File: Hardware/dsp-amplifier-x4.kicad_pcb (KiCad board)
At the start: 4 copper layers, 182 x 90 mm, 167 parts, among them J1 USBi, J10 Conn_Coaxial, J2 EXT, J3 Raspberry_Pi_2_3, J4 Screw_Terminal_01x02, J5 Screw_Terminal_01x02, J6 Screw_Terminal_01x02, J7 Screw_Terminal_01x02, J8 USB_B, J9 Conn_Coaxial, P1 Conn_WallPlug, Q1 STD2805, T1 DA100J, U1 ADAU1452, U10 25LCxxx, U2 TPS54308, U3 TPS54308, U4 AMS1117-3.3, U5 SI53365, U6 TAS5760MDCAR, U7 TAS5760MDCAR, U8 USBLC6-2SC6, U9 PCM2707, X1 ASV-24.576MHz-EJ-T, Y1 12 MHz

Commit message: release candidate 1, drc clean
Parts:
- moved C1 2.83 mm to (98.5, 84.2)
- moved C22 1.77 mm to (98.5, 81.8)
- moved J9 0.75 mm to (89.0, 77.0)
- moved J10 0.25 mm to (73.0, 77.0)
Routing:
- net /DVDD: track 57.4 -> 51.6 mm
- net Net-(C79-Pad1): track 13.6 -> 11.1 mm
- net +3V3: track 119.7 -> 121.7 mm
- net /GAIN0: track 53.6 -> 52.0 mm
- net GND: track 240.5 -> 239.4 mm
- net +3.3VA: track 30.6 -> 30.5 mm, vias 17 -> 18

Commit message: new sockets
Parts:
- J4, J5, J6, J7, P1: footprint TerminalBlock:TerminalBlock_Wuerth_691311400102_P7.62mm -> terminal_connectors:wuerth_691216410002
- moved P1 4.12 mm to (237.2, 127.0), turned to 270 degrees
- moved J4 4.00 mm to (172.0, 123.5), turned to 90 degrees
- moved J5 4.00 mm to (172.0, 140.5), turned to 90 degrees
- moved J6 3.81 mm to (172.0, 89.1), turned to 90 degrees
- moved J7 3.75 mm to (172.0, 106.0), turned to 90 degrees
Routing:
- net /Power/AC_N: track 33.2 -> 33.8 mm
- net /Power/AC_L: track 21.1 -> 21.7 mm

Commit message: production v0.1 with gerber
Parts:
- added TP1: TestPoint, TestPoint:TestPoint_Pad_D1.0mm, F.Cu at (108.5, 115.0)
- added TP2: NCS, TestPoint:TestPoint_Pad_D1.0mm, F.Cu at (92.0, 142.0)
- added TP3: MISO, TestPoint:TestPoint_Pad_D1.0mm, F.Cu at (91.5, 133.8)
- added TP4: MOSI, TestPoint:TestPoint_Pad_D1.0mm, F.Cu at (94.0, 133.8)
- added TP5: SCLK, TestPoint:TestPoint_Pad_D1.0mm, F.Cu at (89.0, 133.8)
- moved R4 5.59 mm to (104.5, 96.2), turned to 180 degrees
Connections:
- Q1 pad 3: +3.3VA -> +3V3
- R4 pad 1: +3.3VA -> +3V3
- U1 pad 23: (no net) -> Net-(TP1-Pad1)
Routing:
- net Net-(TP1-Pad1): track 0.00 -> 8.83 mm
- net +3.3VA: track 30.5 -> 24.5 mm, vias 18 -> 16
- net /VDRIVE: track 11.1 -> 7.33 mm
- net +3V3: track 121.7 -> 124.7 mm
- net /PI_SCLK0: track 110.1 -> 112.8 mm
- net /PI_MOSI0: track 92.1 -> 94.8 mm
- net /PI_MISO0: track 105.1 -> 107.9 mm
- added copper zone on In2.Cu, net +3.3VA
- added copper zone on In2.Cu, net +3V3
- added copper zone on In2.Cu, net +5VD
- added copper zone on In2.Cu, net /DVDD
- removed copper zone on In1.Cu, net +3.3VA
- removed copper zone on In1.Cu, net +3V3
- removed copper zone on In1.Cu, net +5VD
- removed copper zone on In1.Cu, net /DVDD
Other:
- rule pad_to_mask_clearance: 0.2 -> 0
- board text added: "For 24V DC"
- board text added: "stärga v0.1"
- board text removed: "soundi v0.1"

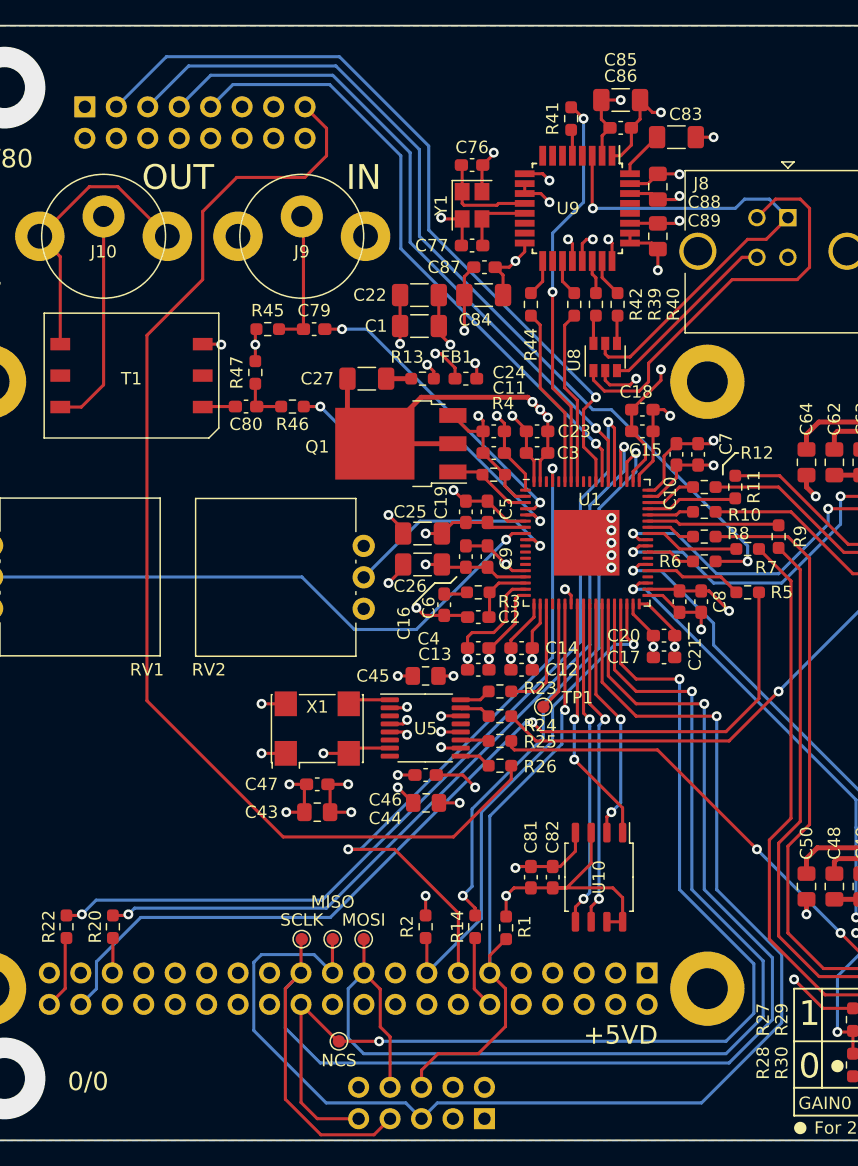
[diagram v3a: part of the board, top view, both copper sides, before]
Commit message: fixed usbi/ext header positions
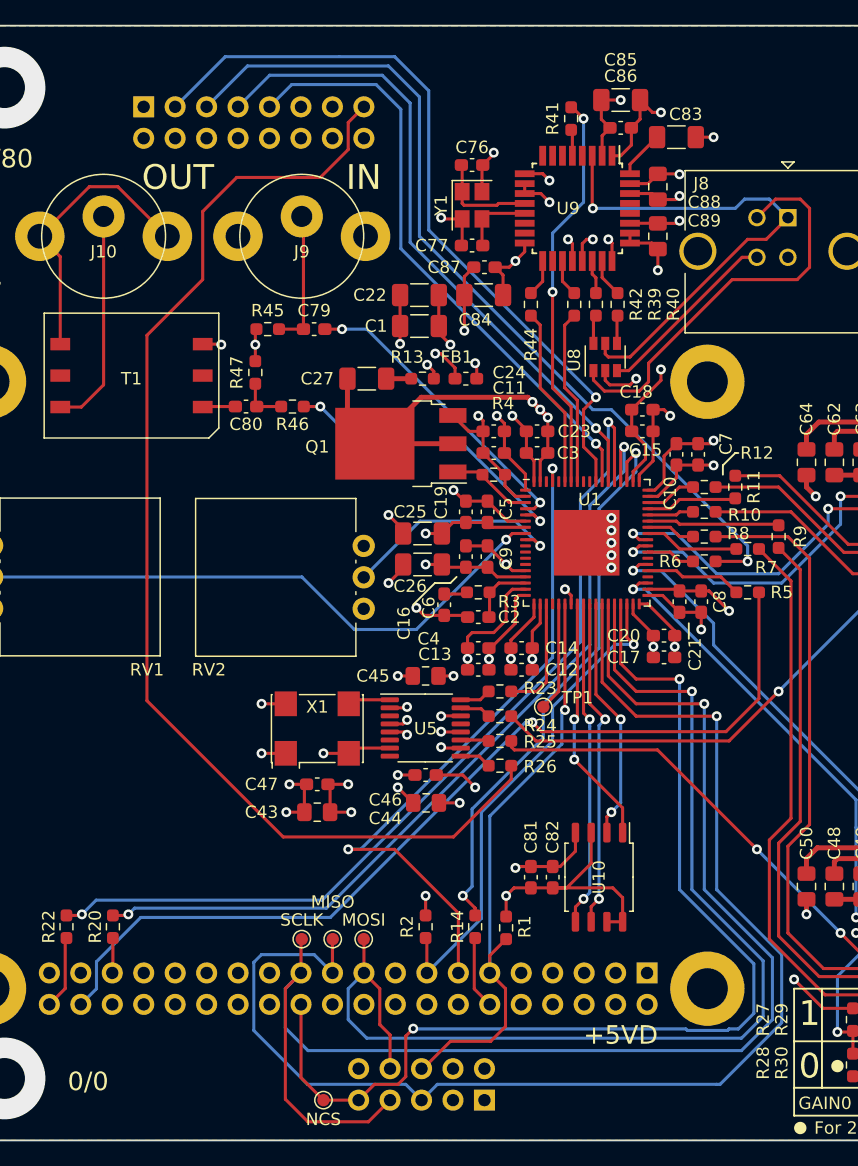
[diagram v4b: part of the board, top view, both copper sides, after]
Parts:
- moved TP2 4.91 mm to (90.8, 146.8)
- moved J2 4.75 mm to (76.2, 66.5)
- moved J1 1.50 mm to (103.8, 146.8)
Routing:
- net +24V: track 126.1 -> 121.5 mm
- net /PI_NCE0: track 91.4 -> 87.7 mm
- net /PI_MOSI0: track 94.8 -> 91.4 mm
- net /EXT_LRCLK: track 51.5 -> 49.0 mm
- net /EXT_BCLK: track 55.5 -> 53.1 mm
- net /EXT_MDO: track 73.8 -> 71.5 mm
- net /EXT_MDI: track 63.4 -> 61.2 mm
- net /DSP_NRESET: track 50.1 -> 48.7 mm
- net /EXT_MCLK: track 94.9 -> 96.1 mm
- net /PI_MISO0: track 107.9 -> 106.7 mm
- net /PI_SCLK0: track 112.8 -> 111.8 mm
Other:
- board text added: "stärga v0.2"
- board text removed: "stärga v0.1"

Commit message: hardware bugfixes
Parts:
- added R33: 1M, Resistor_SMD:R_0603_1608Metric_Pad0.98x0.95mm_HandSolder, F.Cu at (102.8, 74.2)
- added R34: 1.5k, Resistor_SMD:R_0603_1608Metric_Pad0.98x0.95mm_HandSolder, F.Cu at (117.2, 81.5)
- added R40: 1.5k, Resistor_SMD:R_0603_1608Metric_Pad0.98x0.95mm_HandSolder, F.Cu at (103.8, 77.0)
- added U2: TSOP583xx, OptoDevice:Vishay_MINICAST-3Pin, F.Cu at (113.2, 145.2)
- C58, C59, C60, C61, C72, C73, C74, C75: footprint Capacitor_SMD:C_0603_1608Metric_Pad1.08x0.95mm_HandSolder -> Capacitor_SMD:C_0805_2012Metric_Pad1.18x1.45mm_HandSolder
- RV1, RV2: footprint Potentiometer_THT:Potentiometer_Vishay_248GJ-249GJ_Single_Vertical -> Potentiometer_THT:Potentiometer_Bourns_PTV09A-1_Single_Vertical
- moved RV1 13.3 mm to (76.2, 102.0), turned to 180 degrees
- moved C76 3.02 mm to (100.0, 70.0)
- moved C77 3.02 mm to (100.0, 76.5)
- moved Y1 3.02 mm to (100.0, 73.2)
- moved C88 2.01 mm to (107.2, 128.8)
- moved C16 1.75 mm to (104.0, 102.9)
- moved C9 1.75 mm to (102.2, 102.9)
- moved C87 1.50 mm to (109.0, 128.8)
- moved C59 0.29 mm to (165.8, 126.3)
- moved C60 0.29 mm to (165.8, 141.5)
- moved C58 0.25 mm to (165.8, 122.2)
- moved C61 0.25 mm to (165.8, 137.5)
- moved C72 0.25 mm to (165.8, 88.0)
- moved C73 0.25 mm to (165.8, 92.0)
- moved C74 0.25 mm to (165.8, 107.2)
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- renumbered C83 to C78, C84 to C79, C85 to C80, C86 to C81, C87 to C82, C88 to C83, C89 to C84, C79 to C85, C80 to C86, C81 to C87, C82 to C88, R20 to R15, R22 to R16, R23 to R17, R24 to R18, R25 to R19, R26 to R20, R27 to R21, R28 to R22, R29 to R23, R30 to R24, R31 to R25, R32 to R26, R33 to R27, R34 to R28, R35 to R29, R36 to R30, R37 to R31, R38 to R32, R39 to R35, R40 to R36, R41 to R37, R42 to R38, R44 to R39, R45 to R41, R46 to R42, R47 to R43, U9 to U10, U10 to U11, U2 to U3, U3 to U4, U4 to U5, U5 to U6, U6 to U7, U7 to U8, U8 to U9
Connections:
- J2 pad 1: +24V -> +5VA
- J3 pad 1: (no net) -> PI_3V3
- J3 pad 3: (no net) -> /IR_INPUT
- U10 pad 11: +3V3 -> (no net)
- U10 pad 15: (no net) -> Net-(R40-Pad1)
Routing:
- net +5VA: track 26.3 -> 218.9 mm, vias 0 -> 3
- net +24V: track 121.5 -> 37.6 mm
- net GND: track 239.4 -> 228.1 mm, vias 116 -> 115
- net PI_3V3: track 0.00 -> 10.4 mm
- net /VPOT0: track 48.0 -> 38.5 mm
- net /IR_INPUT: track 0.00 -> 9.35 mm
- net Net-(C76-Pad1): track 8.30 -> 11.4 mm
- net Net-(C77-Pad1): track 5.81 -> 8.71 mm
- net Net-(R40-Pad1): track 0.00 -> 2.44 mm
- net /EXT_MCLK: track 96.1 -> 94.1 mm
- net +3V3: track 124.7 -> 122.7 mm, vias 29 -> 30
- net /USB I2S/USB-DP: track 3.11 -> 4.98 mm
- net /PI_MISO0: track 106.7 -> 107.9 mm
- net Net-(C33-Pad1): track 8.22 -> 7.00 mm
- net Net-(C32-Pad1): track 8.22 -> 7.00 mm
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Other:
- board text added: "+5VA supplied"
- board text added: "IR RX"
- board text added: "stärga v1"
- board text removed: "stärga v0.2"

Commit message: various bugfixes
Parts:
- removed TP1: TestPoint, TestPoint:TestPoint_Pad_D1.0mm
- removed TP2: NCS, TestPoint:TestPoint_Pad_D1.0mm
- removed TP3: MISO, TestPoint:TestPoint_Pad_D1.0mm
- removed TP4: MOSI, TestPoint:TestPoint_Pad_D1.0mm
- removed TP5: SCLK, TestPoint:TestPoint_Pad_D1.0mm
- FB1: value 600/100M -> BLM18SP601SZ1D (600/100M)
- RV1, RV2: value R_POT -> PTV09A-1020F-B203
- moved FB1 2.83 mm to (100.2, 86.5)
- moved U2 2.25 mm to (115.5, 145.2)
- moved C53 0.75 mm to (149.8, 115.5)
- moved C83 0.50 mm to (117.8, 72.5)
- turned R33 to 90 degrees
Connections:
- R33 pad 1: Net-(C76-Pad1) -> Net-(C77-Pad1)
- R33 pad 2: Net-(C77-Pad1) -> Net-(C76-Pad1)
- R34 pad 2: +3V3 -> VBUS
- U1 pad 23: Net-(TP1-Pad1) -> (no net)
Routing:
- net Net-(TP1-Pad1): track 8.83 -> 0.00 mm
- net /PI_SCLK0: track 112.4 -> 105.8 mm
- net +5VA: track 218.9 -> 225.4 mm, vias 3 -> 5
- net /PI_MOSI0: track 92.2 -> 86.7 mm
- net /SPDIF_IN: track 24.6 -> 28.4 mm
- net GND: track 228.1 -> 225.7 mm, vias 115 -> 116
- net VBUS: track 41.3 -> 43.3 mm
- net /PI_NCE0: track 88.5 -> 89.6 mm, vias 2 -> 1
- net PI_3V3: track 10.4 -> 11.3 mm
- net /IR_INPUT: track 9.35 -> 10.3 mm
- net +3V3: track 122.7 -> 121.9 mm, vias 30 -> 31
- net /PI_MISO0: track 107.9 -> 107.3 mm
- net /AMP1_NSPK_SD: track 41.0 -> 40.4 mm
- net +3.3VA: track 24.5 -> 24.6 mm, vias 16 -> 18
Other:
- board text added: "VAUX0"
- board text added: "VAUX1"

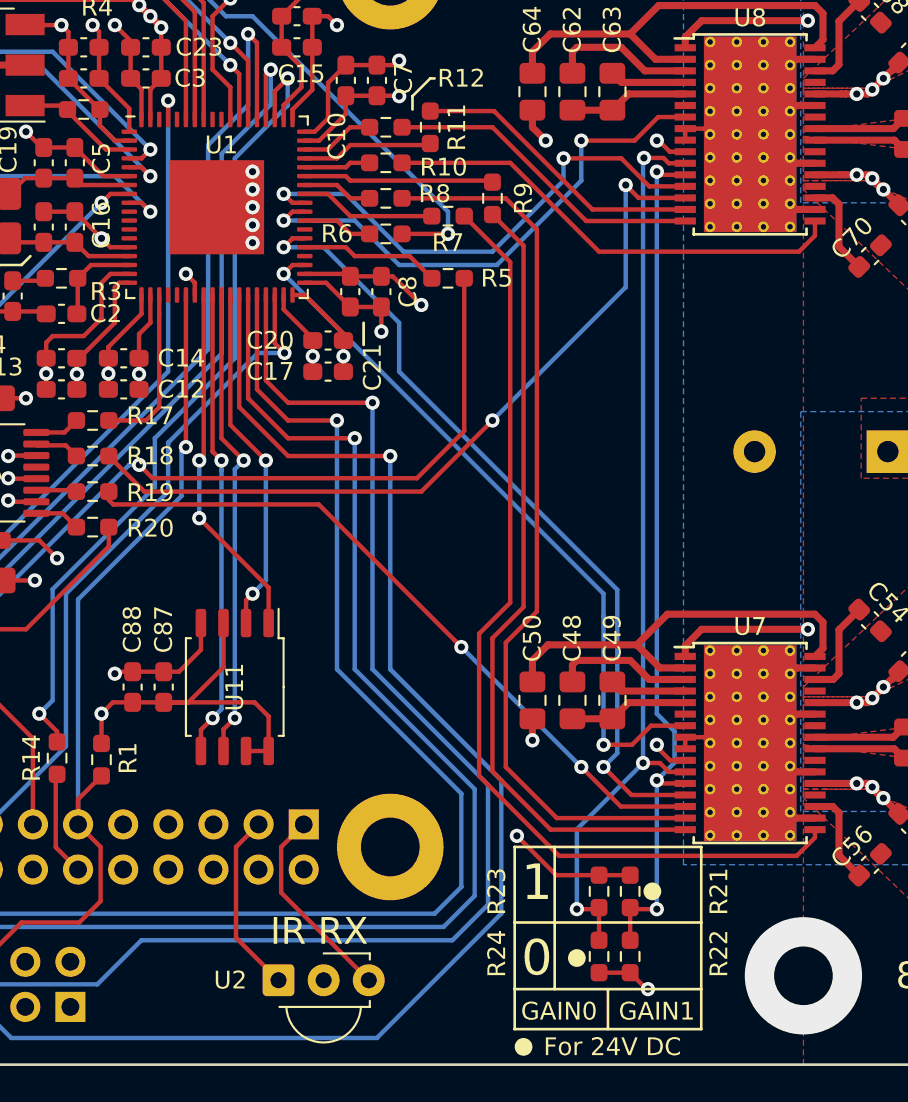
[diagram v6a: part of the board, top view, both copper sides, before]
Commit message: software gain control
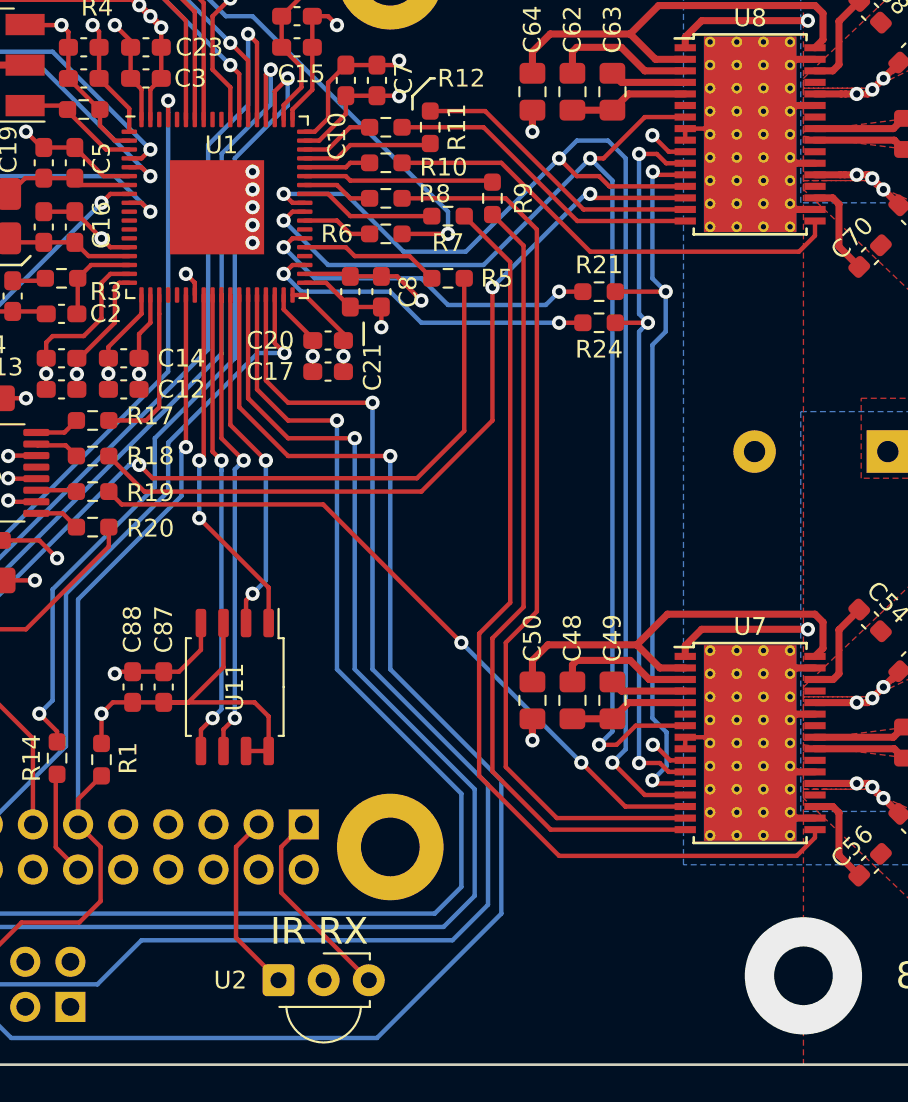
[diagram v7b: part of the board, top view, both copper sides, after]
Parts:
- removed R22, R23: DNP, Resistor_SMD:R_0603_1608Metric_Pad0.98x0.95mm_HandSolder
- moved R24 35.7 mm to (133.5, 108.2), turned to 180 degrees
- moved R21 33.8 mm to (133.5, 106.5), turned to 180 degrees
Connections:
- R21 pad 2: +3V3 -> /GAIN1_OUT
- R24 pad 1: GND -> /GAIN0
- R24 pad 2: /GAIN0 -> /GAIN0_OUT
- U1 pad 39: /AMP1_NSPK_SD -> /GAIN0_OUT
- U1 pad 42: /AMP1_SPK_SLEEP -> /GAIN1_OUT
- U1 pad 45: /AMP2_NSPK_SD -> /AMP_NSPK_SD
- U1 pad 46: /AMP2_SPK_SLEEP -> /AMP_SPK_SLEEP
- U7 pad 13: /AMP1_SPK_SLEEP -> /AMP_SPK_SLEEP
- U7 pad 7: /AMP1_NSPK_SD -> /AMP_NSPK_SD
- U8 pad 13: /AMP2_SPK_SLEEP -> /AMP_SPK_SLEEP
- U8 pad 7: /AMP2_NSPK_SD -> /AMP_NSPK_SD
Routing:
- net /AMP_SPK_SLEEP: track 0.00 -> 71.9 mm, vias 0 -> 3
- net /AMP_NSPK_SD: track 0.00 -> 67.6 mm, vias 0 -> 3
- net /AMP1_SPK_SLEEP: track 45.3 -> 0.00 mm, vias 2 -> 0
- net /AMP1_NSPK_SD: track 40.4 -> 0.00 mm, vias 2 -> 0
- net /AMP2_NSPK_SD: track 29.8 -> 0.00 mm, vias 2 -> 0
- net /AMP2_SPK_SLEEP: track 28.9 -> 0.00 mm, vias 2 -> 0
- net /GAIN1_OUT: track 0.00 -> 19.9 mm, vias 0 -> 2
- net /GAIN0_OUT: track 0.00 -> 19.4 mm, vias 0 -> 2
- net /GAIN0: track 52.0 -> 42.2 mm
- net +3V3: track 121.9 -> 115.1 mm, vias 31 -> 30
- net /GAIN1: track 49.0 -> 42.2 mm
- net GND: track 225.7 -> 221.5 mm, vias 116 -> 115
- net /AMP2_CLOCK: track 44.1 -> 44.7 mm
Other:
- board text removed: "0"
- board text removed: "1"
- board text removed: "For 24V DC"
- board text removed: "GAIN0"
- board text removed: "GAIN1"

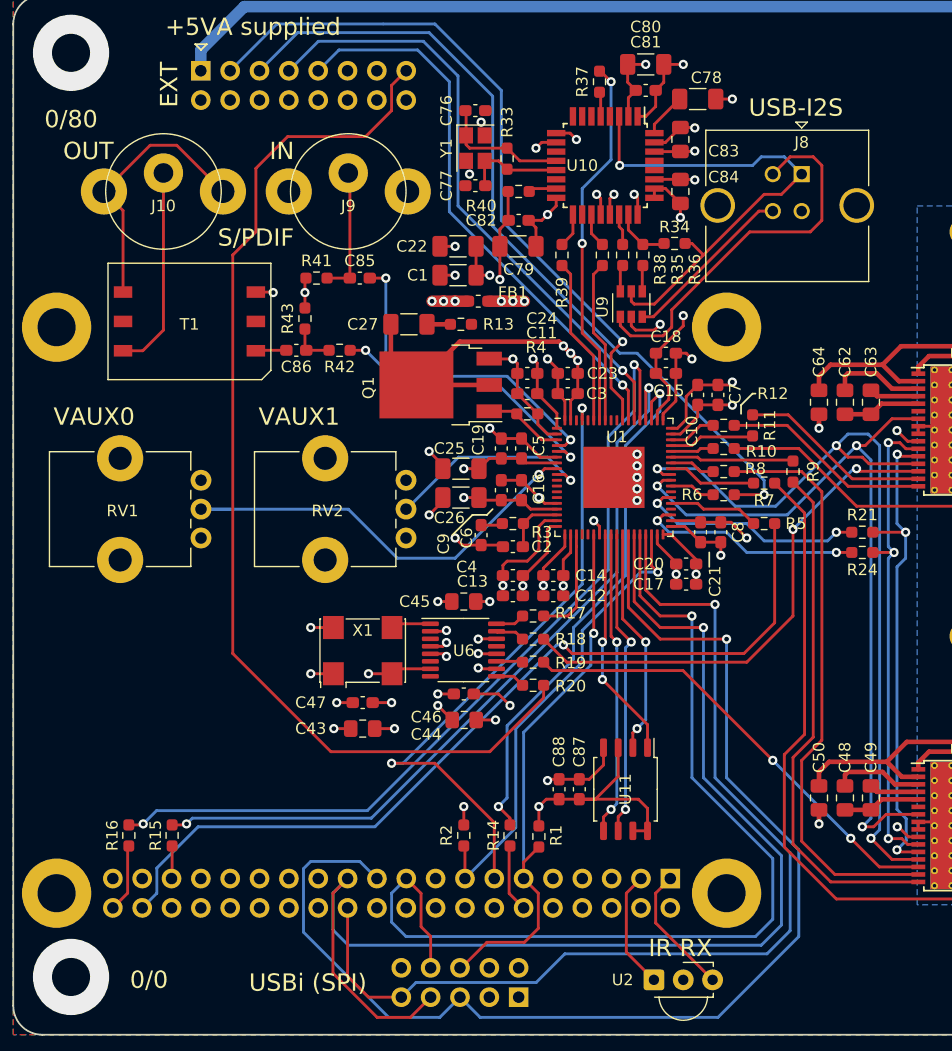
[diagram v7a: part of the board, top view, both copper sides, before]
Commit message: connect pi i2c to header
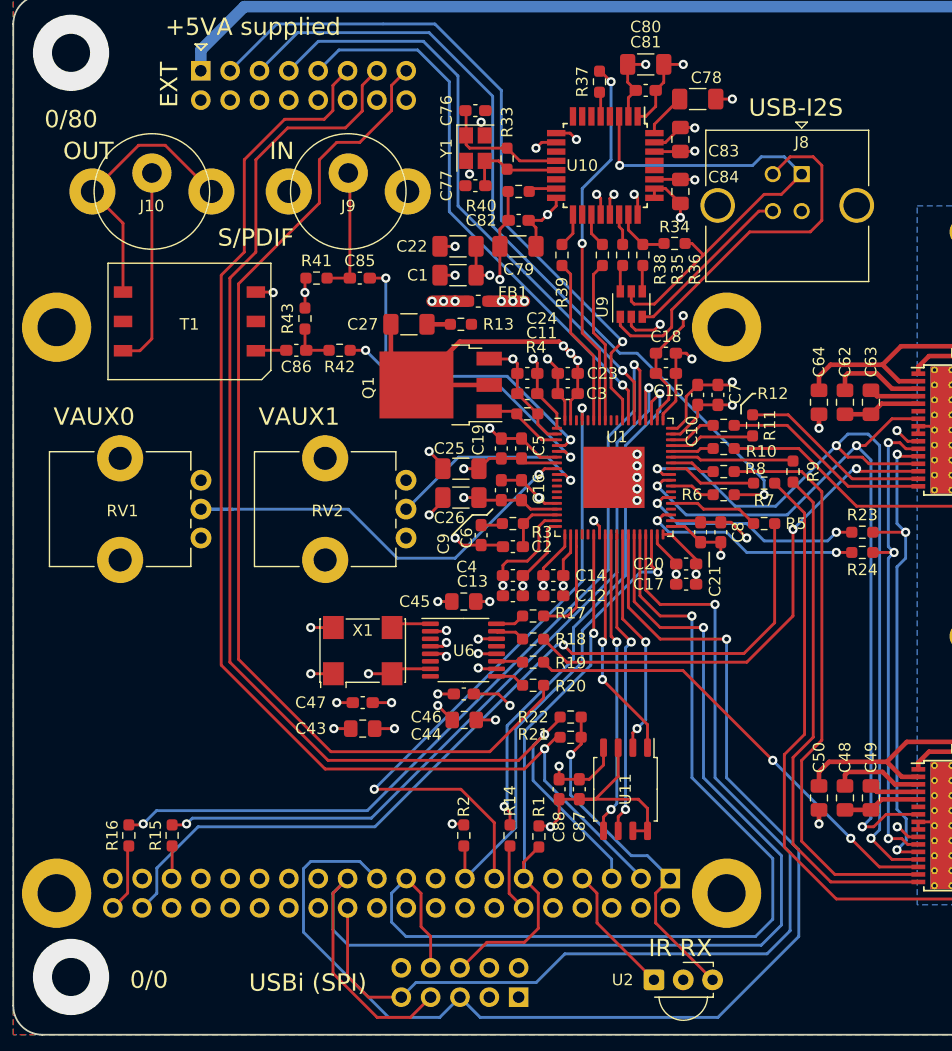
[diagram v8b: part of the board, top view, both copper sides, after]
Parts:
- added R21: 4.3k, Resistor_SMD:R_0603_1608Metric_Pad0.98x0.95mm_HandSolder, F.Cu at (108.2, 124.2)
- added R22: 4.3k, Resistor_SMD:R_0603_1608Metric_Pad0.98x0.95mm_HandSolder, F.Cu at (108.2, 122.5)
- moved J10 1.00 mm to (72.0, 77.0)
- renumbered R21 to R23
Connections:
- J2 pad 11: (no net) -> /PI_SDA
- J2 pad 13: (no net) -> /PI_SCL
- J3 pad 3: /IR_INPUT -> /PI_SDA
- J3 pad 5: (no net) -> /PI_SCL
- J3 pad 7: (no net) -> /IR_INPUT
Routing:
- net /PI_SCL: track 0.00 -> 108.9 mm, vias 0 -> 1
- net /PI_SDA: track 0.00 -> 106.9 mm, vias 0 -> 1
- net PI_3V3: track 11.3 -> 30.4 mm, vias 0 -> 1
- net /EXT_MCLK: track 94.1 -> 90.9 mm
- net /PI_MUTE: track 55.3 -> 58.2 mm
- net /IR_INPUT: track 10.3 -> 11.3 mm
- net +3V3: track 115.1 -> 114.6 mm
